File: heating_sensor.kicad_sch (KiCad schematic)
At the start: 3 parts

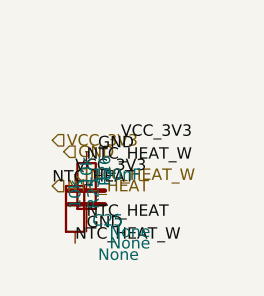
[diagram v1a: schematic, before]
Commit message: fix router map cell no more mark for pins
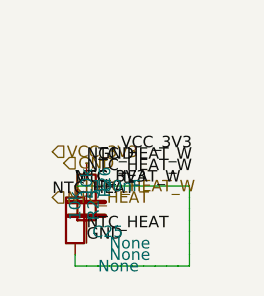
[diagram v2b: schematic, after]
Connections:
- net NTC_HEAT_W: now also R26.1

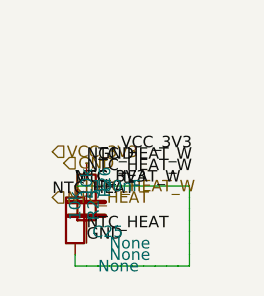
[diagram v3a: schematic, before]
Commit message: исправлены метки
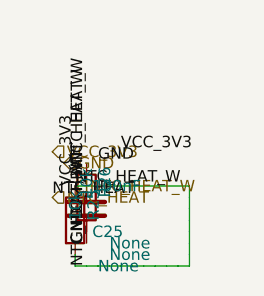
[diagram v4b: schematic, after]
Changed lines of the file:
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@@
 		(instances
 			(project "Untitled"
-				(path "/79af6f5e-7885-4024-8b29-e52190de7308"
+				(path "/51987713-8abd-43cc-8dc0-832c464dab57"
 					(reference "C25")
 					(unit 1)
@@
 		(instances
 			(project "Untitled"
-				(path "/79af6f5e-7885-4024-8b29-e52190de7308"
+				(path "/51987713-8abd-43cc-8dc0-832c464dab57"
 					(reference "R25")
 					(unit 1)
@@
 		(instances
 			(project "Untitled"
-				(path "/79af6f5e-7885-4024-8b29-e52190de7308"
+				(path "/51987713-8abd-43cc-8dc0-832c464dab57"
 					(reference "R26")
 					(unit 1)
@@
 	)
 	(label "VCC_3V3"
-		(at 16.51 15.24 0)
+		(at 16.51 15.24 90)
 		(effects
 			(font
@@
 	)
 	(label "VCC_3V3"
-		(at 21.59 11.43 0)
+		(at 21.59 11.43 180)
 		(effects
 			(font
@@
 	)
 	(label "GND"
-		(at 17.78 21.59 0)
+		(at 17.78 21.59 270)
 		(effects
 			(font
@@
 	)
 	(label "GND"
-		(at 19.05 12.7 0)
+		(at 19.05 12.7 180)
 		(effects
 			(font
@@
 	)
 	(label "NTC_HEAT_W"
-		(at 17.78 13.97 0)
+		(at 17.78 13.97 90)
 		(effects
 			(font
@@
 	)
 	(label "NTC_HEAT_W"
-		(at 17.78 12.7 0)
+		(at 17.78 12.7 90)
 		(effects
 			(font
@@
 	)
 	(label "NTC_HEAT_W"
-		(at 16.51 15.24 0)
+		(at 16.51 15.24 0.0000)
+		(effects
+			(font
+				(size 1.27 1.27)
+			)
+			(justify left bottom)
+		)
+	)
+	(label "NTC_HEAT_W"
+		(at 17.78 24.13 90)
 		(effects
 			(font
@@
 	)
 	(label "NTC_HEAT"
-		(at 17.78 20.32 0)
+		(at 17.78 20.32 270)
 		(effects
 			(font
@@
 	)
 	(label "NTC_HEAT"
-		(at 13.97 16.51 0)
-		(effects
-			(font
+		(at 13.97 16.51 0.0000)
+		(effects
+			(font

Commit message: fix writer
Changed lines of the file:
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@@
 		(instances
 			(project "Untitled"
-				(path "/51987713-8abd-43cc-8dc0-832c464dab57"
+				(path "/c49ef74a-788a-4bab-9f15-e22212d1716d"
 					(reference "C25")
 					(unit 1)
@@
 		(instances
 			(project "Untitled"
-				(path "/51987713-8abd-43cc-8dc0-832c464dab57"
+				(path "/c49ef74a-788a-4bab-9f15-e22212d1716d"
 					(reference "R25")
 					(unit 1)
@@
 		(instances
 			(project "Untitled"
-				(path "/51987713-8abd-43cc-8dc0-832c464dab57"
+				(path "/c49ef74a-788a-4bab-9f15-e22212d1716d"
 					(reference "R26")
 					(unit 1)
@@
 	(wire
 		(pts
-			(xy 16.51 24.13) (xy 17.78 24.13)
-		)
-		(stroke
-			(width 0)
-			(type default)
-		)
-	)
-	(wire
-		(pts
-			(xy 17.78 24.13) (xy 19.05 24.13)
-		)
-		(stroke
-			(width 0)
-			(type default)
-		)
-	)
-	(wire
-		(pts
-			(xy 19.05 24.13) (xy 20.32 24.13)
-		)
-		(stroke
-			(width 0)
-			(type default)
-		)
-	)
-	(wire
-		(pts
-			(xy 20.32 24.13) (xy 21.59 24.13)
-		)
-		(stroke
-			(width 0)
-			(type default)
-		)
-	)
-	(wire
-		(pts
-			(xy 21.59 24.13) (xy 22.86 24.13)
-		)
-		(stroke
-			(width 0)
-			(type default)
-		)
-	)
-	(wire
-		(pts
-			(xy 22.86 24.13) (xy 24.13 24.13)
-		)
-		(stroke
-			(width 0)
-			(type default)
-		)
-	)
-	(wire
-		(pts
-			(xy 24.13 24.13) (xy 25.4 24.13)
-		)
-		(stroke
-			(width 0)
-			(type default)
-		)
-	)
-	(wire
-		(pts
-			(xy 25.4 24.13) (xy 26.67 24.13)
-		)
-		(stroke
-			(width 0)
-			(type default)
-		)
-	)
-	(wire
-		(pts
-			(xy 26.67 24.13) (xy 27.94 24.13)
-		)
-		(stroke
-			(width 0)
-			(type default)
-		)
-	)
-	(wire
-		(pts
-			(xy 27.94 24.13) (xy 29.21 24.13)
-		)
-		(stroke
-			(width 0)
-			(type default)
-		)
-	)
-	(wire
-		(pts
-			(xy 29.21 24.13) (xy 29.21 22.86)
-		)
-		(stroke
-			(width 0)
-			(type default)
-		)
-	)
-	(wire
-		(pts
-			(xy 29.21 22.86) (xy 29.21 21.59)
-		)
-		(stroke
-			(width 0)
-			(type default)
-		)
-	)
-	(wire
-		(pts
-			(xy 29.21 21.59) (xy 29.21 20.32)
-		)
-		(stroke
-			(width 0)
-			(type default)
-		)
-	)
-	(wire
-		(pts
-			(xy 29.21 20.32) (xy 29.21 19.05)
-		)
-		(stroke
-			(width 0)
-			(type default)
-		)
-	)
-	(wire
-		(pts
-			(xy 29.21 19.05) (xy 29.21 17.78)
-		)
-		(stroke
-			(width 0)
-			(type default)
-		)
-	)
-	(wire
-		(pts
-			(xy 29.21 17.78) (xy 29.21 16.51)
-		)
-		(stroke
-			(width 0)
-			(type default)
-		)
-	)
-	(wire
-		(pts
-			(xy 29.21 16.51) (xy 29.21 15.24)
+			(xy 16.51 24.13) (xy 29.21 24.13)
+		)
+		(stroke
+			(width 0)
+			(type default)
+		)
+	)
+	(wire
+		(pts
+			(xy 29.21 24.13) (xy 29.21 15.24)
 		)
 		(stroke
@@
 	(hierarchical_label "VCC_3V3"
 		(shape input)
-		(at 13.97 11.43 180)
+		(at 21.59 11.43 180)
 		(effects
 			(font
@@
 	(hierarchical_label "GND"
 		(shape input)
-		(at 15.24 12.7 180)
-		(effects
-			(font
+		(at 19.05 12.7 180)
+		(effects
+			(font

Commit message: fic placer for small schemes
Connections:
- net NTC_HEAT_W: no longer R25.1
- new net VCC_3V3: R25.1
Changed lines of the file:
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@@
 		(instances
 			(project "Untitled"
-				(path "/877ebbf2-9da6-4fab-8a1c-67fe445f8f21"
+				(path "/2b46367b-7f7a-4d0b-a981-14ef6f17f746"
 					(reference "C25")
 					(unit 1)
@@
 	(symbol
 		(lib_id "Device:R")
-		(at 16.51 19.05 0)
+		(at 13.97 17.78 0)
 		(unit 1)
 		(exclude_from_sim no)
@@
 		(fields_autoplaced no)
 		(property "Reference" "R25"
-			(at 18.542 19.05 90)
+			(at 16.002 17.78 90)
 			(effects
 				(font
@@
 		)
 		(property "Value" "10k"
-			(at 16.51 19.05 90)
+			(at 13.97 17.78 90)
 			(effects
 				(font
@@
 		)
 		(property "mirror" "None"
-			(at 19.05 24.1299 0)
+			(at 16.51 22.8599 0)
 			(effects
 				(font
@@
 		(instances
 			(project "Untitled"
-				(path "/877ebbf2-9da6-4fab-8a1c-67fe445f8f21"
+				(path "/2b46367b-7f7a-4d0b-a981-14ef6f17f746"
 					(reference "R25")
 					(unit 1)
@@
 	(symbol
 		(lib_id "Device:R")
-		(at 17.78 16.51 0)
+		(at 21.59 13.97 0)
 		(unit 1)
 		(exclude_from_sim no)
@@
 		(fields_autoplaced no)
 		(property "Reference" "R26"
-			(at 19.812 16.51 90)
+			(at 23.622 13.97 90)
 			(effects
 				(font
@@
 		)
 		(property "Value" "10k"
-			(at 17.78 16.51 90)
+			(at 21.59 13.97 90)
 			(effects
 				(font
@@
 		)
 		(property "mirror" "None"
-			(at 20.32 21.5899 0)
+			(at 24.13 19.0499 0)
 			(effects
 				(font
@@
 		(instances
 			(project "Untitled"
-				(path "/877ebbf2-9da6-4fab-8a1c-67fe445f8f21"
+				(path "/2b46367b-7f7a-4d0b-a981-14ef6f17f746"
 					(reference "R26")
 					(unit 1)
@@
 	(wire
 		(pts
-			(xy 16.51 22.86) (xy 16.51 24.13)
-		)
-		(stroke
-			(width 0)
-			(type default)
-		)
-	)
-	(wire
-		(pts
-			(xy 16.51 24.13) (xy 29.21 24.13)
-		)
-		(stroke
-			(width 0)
-			(type default)
-		)
-	)
-	(wire
-		(pts
-			(xy 29.21 24.13) (xy 29.21 15.24)
-		)
-		(stroke
-			(width 0)
-			(type default)
-		)
-	)
-	(wire
-		(pts
-			(xy 29.21 15.24) (xy 16.51 15.24)
-		)
-		(stroke
-			(width 0)
-			(type default)
-		)
-	)
-	(label "VCC_3V3"
-		(at 16.51 15.24 90)
-		(effects
-			(font
-				(size 1.27 1.27)
-			)
-			(justify left bottom)
-		)
-	)
-	(label "VCC_3V3"
-		(at 21.59 11.43 180)
-		(effects
-			(font
-				(size 1.27 1.27)
-			)
-			(justify left bottom)
-		)
-	)
-	(label "GND"
-		(at 17.78 21.59 270)
-		(effects
-			(font
-				(size 1.27 1.27)
-			)
-			(justify left bottom)
-		)
-	)
-	(label "GND"
-		(at 19.05 12.7 180)
-		(effects
-			(font
-				(size 1.27 1.27)
-			)
-			(justify left bottom)
-		)
+			(xy 13.97 13.97) (xy 13.97 12.7)
+		)
+		(stroke
+			(width 0)
+			(type default)
+		)
+	)
+	(wire
+		(pts
+			(xy 13.97 12.7) (xy 10.16 12.7)
+		)
+		(stroke
+			(width 0)
+			(type default)
+		)
+	)
+	(wire
+		(pts
+			(xy 10.16 12.7) (xy 10.16 8.89)
+		)
+		(stroke
+			(width 0)
+			(type default)
+		)
+	)
+	(wire
+		(pts
+			(xy 10.16 8.89) (xy 19.05 8.89)
+		)
+		(stroke
+			(width 0)
+			(type default)
+		)
+	)
+	(wire
+		(pts
+			(xy 17.78 21.59) (xy 17.78 22.86)
+		)
+		(stroke
+			(width 0)
+			(type default)
+		)
+	)
+	(wire
+		(pts
+			(xy 17.78 22.86) (xy 11.43 22.86)
+		)
+		(stroke
+			(width 0)
+			(type default)
+		)
+	)
+	(wire
+		(pts
+			(xy 11.43 22.86) (xy 11.43 11.43)
+		)
+		(stroke
+			(width 0)
+			(type default)
+		)
+	)
+	(wire
+		(pts
+			(xy 11.43 11.43) (xy 13.97 11.43)
+		)
+		(stroke
+			(width 0)
+			(type default)
+		)
+	)
+	(wire
+		(pts
+			(xy 13.97 11.43) (xy 19.05 11.43)
+		)
+		(stroke
+			(width 0)
+			(type default)
+		)
+	)
+	(wire
+		(pts
+			(xy 13.97 21.59) (xy 13.97 24.13)
+		)
+		(stroke
+			(width 0)
+			(type default)
+		)
+	)
+	(wire
+		(pts
+			(xy 13.97 24.13) (xy 33.02 24.13)
+		)
+		(stroke
+			(width 0)
+			(type default)
+		)
+	)
+	(wire
+		(pts
+			(xy 33.02 24.13) (xy 33.02 19.05)
+		)
+		(stroke
+			(width 0)
+			(type default)
+		)
+	)
+	(wire
+		(pts
+			(xy 33.02 19.05) (xy 20.32 19.05)
+		)
+		(stroke
+			(width 0)
+			(type default)
+		)
+	)
+	(wire
+		(pts
+			(xy 21.59 10.16) (xy 21.59 8.89)
+		)
+		(stroke
+			(width 0)
+			(type default)
+		)
+	)
+	(wire
+		(pts
+			(xy 21.59 8.89) (xy 33.02 8.89)
+		)
+		(stroke
+			(width 0)
+			(type default)
+		)
+	)
+	(wire
+		(pts
+			(xy 33.02 8.89) (xy 33.02 21.59)
+		)
+		(stroke
+			(width 0)
+			(type default)
+		)
+	)
+	(wire
+		(pts
+			(xy 33.02 21.59) (xy 30.48 21.59)
+		)
+		(stroke
+			(width 0)
+			(type default)
+		)
+	)
+	(wire
+		(pts
+			(xy 30.48 21.59) (xy 30.48 24.13)
+		)
+		(stroke
+			(width 0)
+			(type default)
+		)
+	)
+	(wire
+		(pts
+			(xy 30.48 24.13) (xy 21.59 24.13)
+		)
+		(stroke
+			(width 0)
+			(type default)
+		)
+	)
+	(junction
+		(at 21.59 24.13)
+		(diameter 0)
+		(color 0 0 0 0)
 	)
 	(label "NTC_HEAT_W"
@@
 	)
 	(label "NTC_HEAT_W"
-		(at 17.78 12.7 90)
+		(at 21.59 10.16 90)
 		(effects
 			(font
@@
 	)
 	(label "NTC_HEAT_W"
-		(at 16.51 15.24 0.0000)
+		(at 20.32 19.05 0.0000)
 		(effects
 			(font
@@
 	)
 	(label "NTC_HEAT"
-		(at 17.78 20.32 270)
+		(at 21.59 17.78 270)
 		(effects
 			(font
@@
 	)
 	(label "NTC_HEAT"
-		(at 13.97 16.51 0.0000)
+		(at 20.32 21.59 0.0000)
 		(effects
 			(font
@@
 	(hierarchical_label "VCC_3V3"
 		(shape input)
-		(at 21.59 11.43 180)
+		(at 19.05 8.89 180)
 		(effects
 			(font
@@
 	(hierarchical_label "GND"
 		(shape input)
-		(at 19.05 12.7 180)
+		(at 19.05 11.43 180)
 		(effects
 			(font
@@
 	(hierarchical_label "NTC_HEAT_W"
 		(shape input)
-		(at 16.51 15.24 0)
+		(at 20.32 19.05 0)
 		(effects
 			(font
@@
 	(hierarchical_label "NTC_HEAT"
 		(shape input)
-		(at 13.97 16.51 0)
-		(effects
-			(font
+		(at 20.32 21.59 0)
+		(effects
+			(font
